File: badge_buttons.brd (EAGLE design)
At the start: 83 x 66 mm, 6 parts

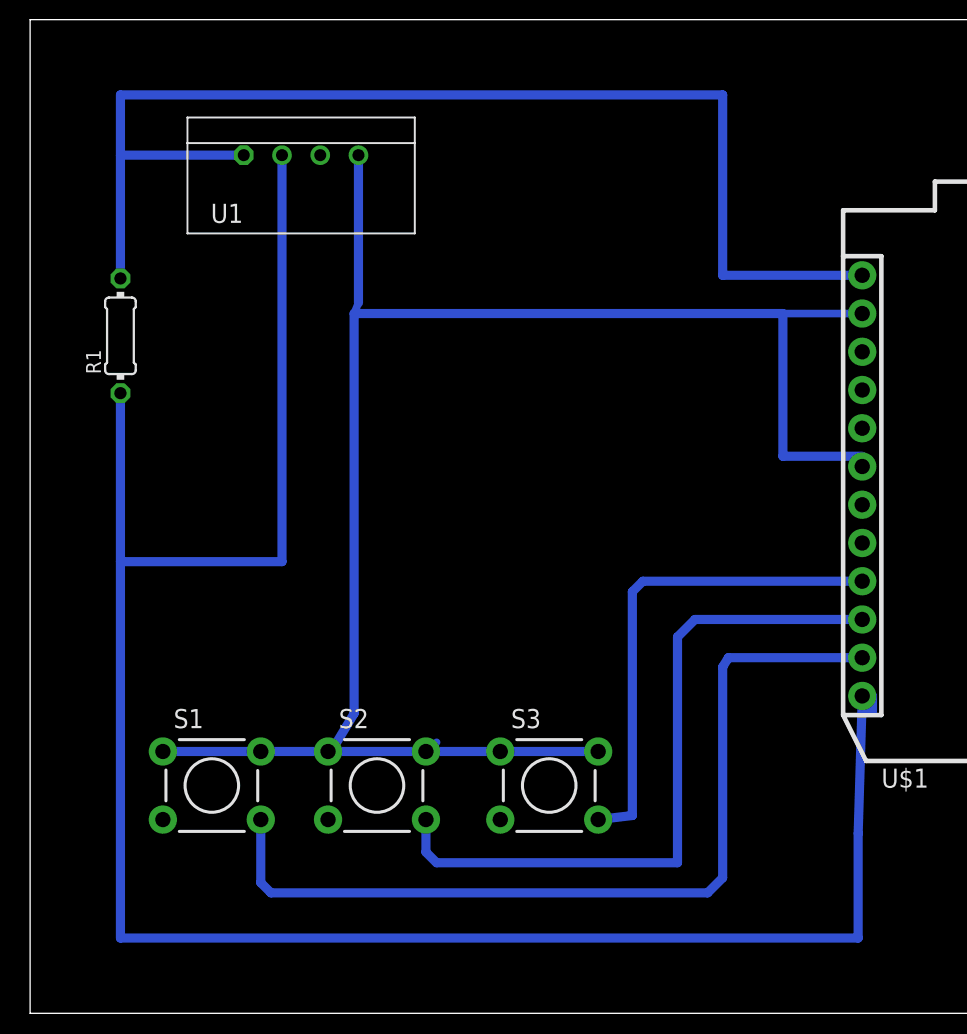
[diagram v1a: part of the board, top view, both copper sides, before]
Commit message: clean up lines, add sensor loop
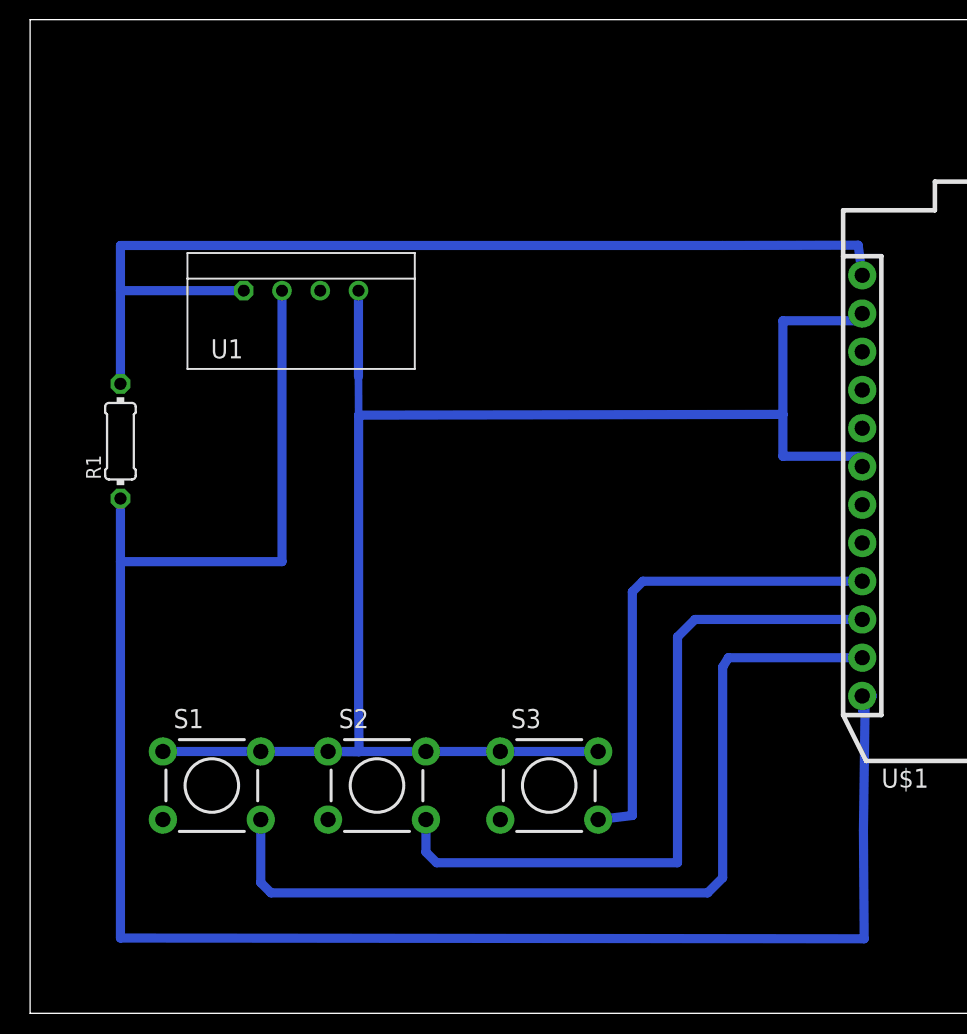
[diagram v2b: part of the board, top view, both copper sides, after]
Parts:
- moved U1 9.00 mm to (28.0, 58.0)
- moved R1 7.00 mm to (16.0, 48.0)
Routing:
- net N$6: track 142.2 -> 127.1 mm
- net N$5: track 81.6 -> 68.4 mm
- net N$4: track 119.1 -> 110.4 mm
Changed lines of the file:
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@@
 <setting verticaltext="up"/>
 </settings>
-<grid distance="1" unitdist="mm" unit="mm" style="lines" multiple="10" display="yes" altdistance="5" altunitdist="mil" altunit="mm"/>
+<grid distance="0.05" unitdist="mm" unit="mm" style="lines" multiple="10" display="yes" altdistance="0.1" altunitdist="mm" altunit="mm"/>
 <layers>
 <layer number="1" name="Top" color="4" fill="1" visible="yes" active="yes"/>
@@
 <element name="S3" library="SparkFun-Retired" package="TACTILE-PTH" value="" x="44.48" y="25.13"/>
 <element name="U$1" library="Particle-Devices" package="PHOTON" value="PHOTON_WITH_HEADERS" x="64" y="26"/>
-<element name="U1" library="RHT03_DHT-22_AM2302" package="RHT03_DHT-22" value="" x="28" y="67">
-<attribute name="PROD_ID" value="SEN-10167" x="28" y="67" size="1.778" layer="27" display="off"/>
+<element name="U1" library="RHT03_DHT-22_AM2302" package="RHT03_DHT-22" value="" x="28" y="58">
+<attribute name="PROD_ID" value="SEN-10167" x="28" y="58" size="1.778" layer="27" display="off"/>
 </element>
-<element name="R1" library="resistor" library_urn="urn:adsk.eagle:library:348" package="0204/7" package3d_urn="urn:adsk.eagle:package:25945/1" value="" x="16" y="55" rot="R90"/>
+<element name="R1" library="resistor" library_urn="urn:adsk.eagle:library:348" package="0204/7" package3d_urn="urn:adsk.eagle:package:25945/1" value="" x="16" y="48" rot="R90"/>
 </elements>
 <signals>
@@
 <wire x1="29.7888" y1="27.3906" x2="30" y2="27.3906" width="0.508" layer="16"/>
 <wire x1="30" y1="27.3906" x2="36.2912" y2="27.3906" width="0.6096" layer="16"/>
-<wire x1="37" y1="28" x2="36.3906" y2="27.3906" width="0.508" layer="16"/>
-<wire x1="36.3906" y1="27.3906" x2="36.2912" y2="27.3906" width="0.508" layer="16"/>
-<wire x1="36.2912" y1="27.3906" x2="41.2288" y2="27.3906" width="0.6096" layer="16"/>
+<wire x1="36.4" y1="27.3" x2="36.3906" y2="27.3906" width="0.508" layer="16"/>
+<wire x1="36.2912" y1="27.3906" x2="36.3906" y2="27.3906" width="0.6096" layer="16"/>
+<wire x1="36.3906" y1="27.3906" x2="41.2288" y2="27.3906" width="0.6096" layer="16"/>
 <wire x1="41.2288" y1="27.3906" x2="47.7312" y2="27.3906" width="0.6096" layer="16"/>
-<wire x1="31.81" y1="67" x2="31.81" y2="57.19" width="0.6096" layer="16"/>
-<wire x1="31.81" y1="57.19" x2="31.52" y2="56.48" width="0.508" layer="16"/>
-<wire x1="31.52" y1="56.48" x2="31.52" y2="29.9106" width="0.6096" layer="16"/>
-<wire x1="31.52" y1="29.9106" x2="30" y2="27.3906" width="0.6096" layer="16"/>
+<wire x1="31.81" y1="58" x2="31.81" y2="52.29" width="0.6096" layer="16"/>
+<wire x1="31.81" y1="52.29" x2="31.82" y2="49.73" width="0.508" layer="16"/>
+<wire x1="31.82" y1="49.73" x2="31.82" y2="30.0606" width="0.6096" layer="16"/>
+<wire x1="31.82" y1="30.0606" x2="31.85305" y2="27.371971875" width="0.6096" layer="16"/>
 <contactref element="U$1" pad="6"/>
-<wire x1="65.27" y1="56.48" x2="60" y2="56.48" width="0.508" layer="16"/>
-<wire x1="60" y1="56.48" x2="31.52" y2="56.48" width="0.6096" layer="16"/>
+<wire x1="31.85305" y1="27.371971875" x2="30" y2="27.3906" width="0.6096" layer="16"/>
+<wire x1="60" y1="49.78" x2="31.82" y2="49.73" width="0.6096" layer="16"/>
 <wire x1="65.27" y1="46.32" x2="65.27" y2="47" width="0.508" layer="16"/>
 <wire x1="65.27" y1="47" x2="60" y2="47" width="0.6096" layer="16"/>
-<wire x1="60" y1="47" x2="60" y2="56.48" width="0.6096" layer="16"/>
+<wire x1="60" y1="47" x2="60" y2="49.78" width="0.6096" layer="16"/>
+<wire x1="65.27" y1="56.48" x2="65.27" y2="56" width="0.6096" layer="16"/>
+<wire x1="65.27" y1="56" x2="60" y2="56" width="0.6096" layer="16"/>
+<wire x1="60" y1="56" x2="60" y2="49.78" width="0.6096" layer="16"/>
 </signal>
 <signal name="N$5">
@@
 <contactref element="U$1" pad="1"/>
 <contactref element="R1" pad="2"/>
-<wire x1="24.19" y1="67" x2="16" y2="67" width="0.6096" layer="16"/>
-<wire x1="16" y1="67" x2="16" y2="71" width="0.6096" layer="16"/>
-<wire x1="16" y1="71" x2="56" y2="71" width="0.6096" layer="16"/>
-<wire x1="56" y1="71" x2="56" y2="59.02" width="0.6096" layer="16"/>
-<wire x1="56" y1="59.02" x2="65.27" y2="59.02" width="0.6096" layer="16"/>
-<wire x1="16" y1="67" x2="16" y2="58.81" width="0.6096" layer="16"/>
+<wire x1="24.19" y1="58" x2="16" y2="58" width="0.6096" layer="16"/>
+<wire x1="16" y1="58" x2="16" y2="61" width="0.6096" layer="16"/>
+<wire x1="16" y1="61" x2="56" y2="61" width="0.6096" layer="16"/>
+<wire x1="56" y1="61" x2="65" y2="61.02" width="0.6096" layer="16"/>
+<wire x1="65" y1="61.02" x2="65.27" y2="59.02" width="0.6096" layer="16"/>
+<wire x1="16" y1="58" x2="16" y2="51.81" width="0.6096" layer="16"/>
 </signal>
 <signal name="N$6">
@@
 <contactref element="U$1" pad="12"/>
 <contactref element="R1" pad="1"/>
-<wire x1="26.73" y1="67" x2="26.73" y2="40" width="0.6096" layer="16"/>
+<wire x1="26.73" y1="58" x2="26.73" y2="40" width="0.6096" layer="16"/>
 <wire x1="26.73" y1="40" x2="16" y2="40" width="0.6096" layer="16"/>
 <wire x1="16" y1="40" x2="16" y2="15" width="0.6096" layer="16"/>
-<wire x1="16" y1="15" x2="65" y2="15" width="0.6096" layer="16"/>
+<wire x1="16" y1="15" x2="65.4" y2="14.95" width="0.6096" layer="16"/>
 <wire x1="66" y1="31.08" x2="65.27" y2="31.08" width="0.508" layer="16"/>
-<wire x1="65" y1="15" x2="65" y2="21.952" width="0.6096" layer="16"/>
-<wire x1="65" y1="21.952" x2="65.27" y2="30.952" width="0.6096" layer="16"/>
-<wire x1="65.27" y1="30.952" x2="65.27" y2="30.064" width="0.508" layer="16"/>
-<wire x1="65.27" y1="30.064" x2="66" y2="30.064" width="0.508" layer="16"/>
-<wire x1="66" y1="30.064" x2="66" y2="31.08" width="0.508" layer="16"/>
-<wire x1="16" y1="51.19" x2="16" y2="40" width="0.6096" layer="16"/>
+<wire x1="65.4" y1="14.95" x2="65.35" y2="22.152" width="0.6096" layer="16"/>
+<wire x1="65.35" y1="22.152" x2="65.47" y2="31.152" width="0.6096" layer="16"/>
+<wire x1="65.47" y1="31.152" x2="65.27" y2="30.064" width="0.508" layer="16"/>
+<wire x1="65.27" y1="30.064" x2="65.15" y2="30.964" width="0.508" layer="16"/>
+<wire x1="65.15" y1="30.964" x2="66" y2="31.08" width="0.508" layer="16"/>
+<wire x1="16" y1="44.19" x2="16" y2="40" width="0.6096" layer="16"/>
 </signal>
 </signals>

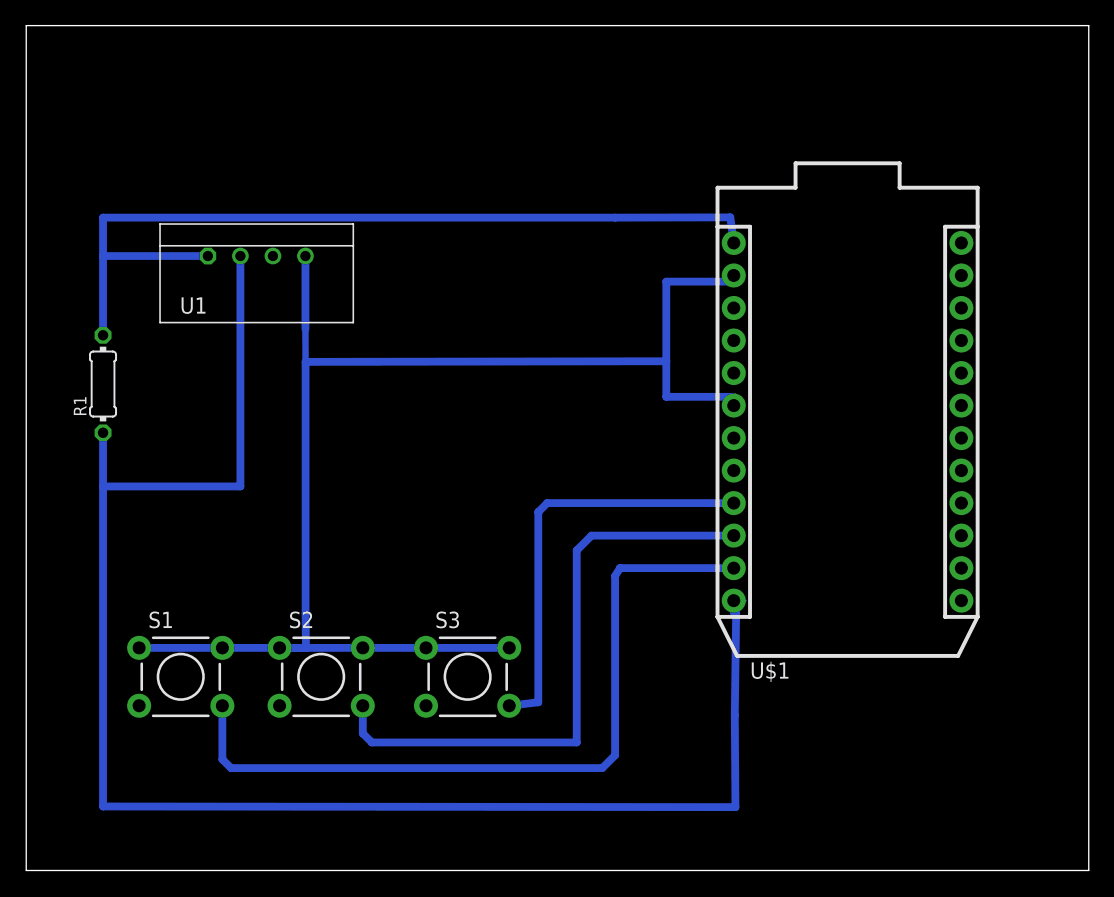
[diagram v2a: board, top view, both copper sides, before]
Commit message: fatten traces
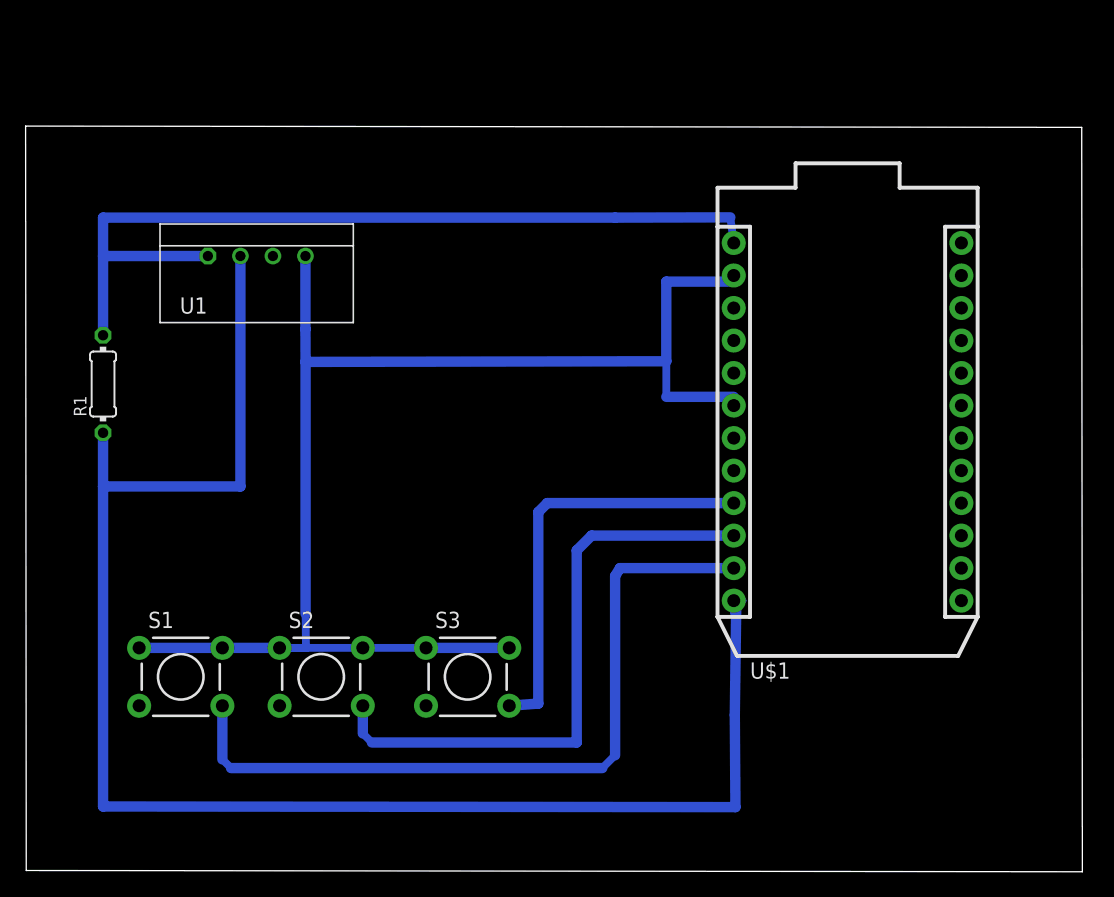
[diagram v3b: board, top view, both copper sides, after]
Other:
- board size 83 x 66 mm -> 82.5 x 58.3 mm
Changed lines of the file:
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@@
 <board>
 <plain>
-<wire x1="10" y1="10" x2="93" y2="10" width="0" layer="20"/>
-<wire x1="93" y1="10" x2="93" y2="76" width="0" layer="20"/>
-<wire x1="93" y1="76" x2="10" y2="76" width="0" layer="20"/>
-<wire x1="10" y1="76" x2="10" y2="10" width="0" layer="20"/>
+<wire x1="10" y1="10" x2="92.5" y2="9.9" width="0" layer="20"/>
+<wire x1="92.5" y1="9.9" x2="92.45" y2="68.05" width="0" layer="20"/>
+<wire x1="92.45" y1="68.05" x2="9.95" y2="68.15" width="0" layer="20"/>
+<wire x1="9.95" y1="68.15" x2="10" y2="10" width="0" layer="20"/>
 </plain>
 <attributes>
@@
 <wire x1="65.27" y1="38.7" x2="65" y2="38.97" width="0.3048" layer="16"/>
 <wire x1="65" y1="38.97" x2="65" y2="39" width="0.3048" layer="16"/>
-<wire x1="47.7312" y1="22.8694" x2="50" y2="23.1382" width="0.6096" layer="16"/>
-<wire x1="50" y1="23.1382" x2="50" y2="38" width="0.6096" layer="16"/>
-<wire x1="50" y1="38" x2="50.7" y2="38.7" width="0.6096" layer="16"/>
-<wire x1="50.7" y1="38.7" x2="65.27" y2="38.7" width="0.6096" layer="16"/>
+<wire x1="47.7312" y1="22.8694" x2="50" y2="23.0382" width="0.8128" layer="16"/>
+<wire x1="50" y1="23.0382" x2="50" y2="38" width="0.8128" layer="16"/>
+<wire x1="50" y1="38" x2="50.7" y2="38.7" width="0.8128" layer="16"/>
+<wire x1="50.7" y1="38.7" x2="65.27" y2="38.7" width="0.8128" layer="16"/>
 </signal>
 <signal name="N$2">
 <contactref element="S2" pad="4"/>
 <contactref element="U$1" pad="10"/>
-<wire x1="36.2912" y1="22.8694" x2="36.2912" y2="20.7088" width="0.6096" layer="16"/>
+<wire x1="36.2912" y1="22.8694" x2="36.2912" y2="20.7088" width="0.8128" layer="16"/>
 <wire x1="36.2912" y1="20.7088" x2="37" y2="20" width="0.6096" layer="16"/>
-<wire x1="37" y1="20" x2="53" y2="20" width="0.6096" layer="16"/>
-<wire x1="53" y1="20" x2="53" y2="35" width="0.6096" layer="16"/>
-<wire x1="54.16" y1="36.16" x2="65.27" y2="36.16" width="0.6096" layer="16"/>
-<wire x1="53" y1="35" x2="54.16" y2="36.16" width="0.6096" layer="16"/>
+<wire x1="37" y1="20" x2="53" y2="20" width="0.8128" layer="16"/>
+<wire x1="53" y1="20" x2="53" y2="35" width="0.8128" layer="16"/>
+<wire x1="54.16" y1="36.16" x2="65.27" y2="36.16" width="0.8128" layer="16"/>
+<wire x1="53" y1="35" x2="54.16" y2="36.16" width="0.8128" layer="16"/>
 </signal>
 <signal name="N$3">
 <contactref element="S1" pad="4"/>
 <contactref element="U$1" pad="11"/>
-<wire x1="25.3212" y1="22.8694" x2="25.3212" y2="18.6788" width="0.6096" layer="16"/>
+<wire x1="25.3212" y1="22.8694" x2="25.3212" y2="18.6788" width="0.8128" layer="16"/>
 <wire x1="25.3212" y1="18.6788" x2="26" y2="18" width="0.6096" layer="16"/>
-<wire x1="26" y1="18" x2="55" y2="18" width="0.6096" layer="16"/>
+<wire x1="26" y1="18" x2="55" y2="18" width="0.8128" layer="16"/>
 <wire x1="55" y1="18" x2="56" y2="19" width="0.6096" layer="16"/>
-<wire x1="56" y1="19" x2="56" y2="33" width="0.6096" layer="16"/>
-<wire x1="56" y1="33" x2="56.38" y2="33.62" width="0.6096" layer="16"/>
-<wire x1="56.38" y1="33.62" x2="65.27" y2="33.62" width="0.6096" layer="16"/>
+<wire x1="56" y1="19" x2="56" y2="33" width="0.8128" layer="16"/>
+<wire x1="56" y1="33" x2="56.38" y2="33.62" width="0.8128" layer="16"/>
+<wire x1="56.38" y1="33.62" x2="65.27" y2="33.62" width="0.8128" layer="16"/>
 </signal>
 <signal name="N$4">
@@
 <contactref element="S2" pad="2"/>
 <contactref element="S3" pad="2"/>
-<wire x1="18.8188" y1="27.3906" x2="25.3212" y2="27.3906" width="0.6096" layer="16"/>
-<wire x1="25.3212" y1="27.3906" x2="29.7888" y2="27.3906" width="0.6096" layer="16"/>
+<wire x1="18.8188" y1="27.3906" x2="25.3212" y2="27.3906" width="0.8128" layer="16"/>
+<wire x1="25.3212" y1="27.3906" x2="29.7888" y2="27.3906" width="0.8128" layer="16"/>
 <wire x1="29.7888" y1="27.3906" x2="30" y2="27.3906" width="0.508" layer="16"/>
 <wire x1="30" y1="27.3906" x2="36.2912" y2="27.3906" width="0.6096" layer="16"/>
@@
 <wire x1="36.2912" y1="27.3906" x2="36.3906" y2="27.3906" width="0.6096" layer="16"/>
 <wire x1="36.3906" y1="27.3906" x2="41.2288" y2="27.3906" width="0.6096" layer="16"/>
-<wire x1="41.2288" y1="27.3906" x2="47.7312" y2="27.3906" width="0.6096" layer="16"/>
-<wire x1="31.81" y1="58" x2="31.81" y2="52.29" width="0.6096" layer="16"/>
-<wire x1="31.81" y1="52.29" x2="31.82" y2="49.73" width="0.508" layer="16"/>
-<wire x1="31.82" y1="49.73" x2="31.82" y2="30.0606" width="0.6096" layer="16"/>
+<wire x1="41.2288" y1="27.3906" x2="47.7312" y2="27.3906" width="0.8128" layer="16"/>
+<wire x1="31.81" y1="58" x2="31.81" y2="52.29" width="0.8128" layer="16"/>
+<wire x1="31.81" y1="52.29" x2="31.82" y2="49.73" width="0.8128" layer="16"/>
+<wire x1="31.82" y1="49.73" x2="31.82" y2="30.0606" width="0.8128" layer="16"/>
 <wire x1="31.82" y1="30.0606" x2="31.85305" y2="27.371971875" width="0.6096" layer="16"/>
 <contactref element="U$1" pad="6"/>
 <wire x1="31.85305" y1="27.371971875" x2="30" y2="27.3906" width="0.6096" layer="16"/>
-<wire x1="60" y1="49.78" x2="31.82" y2="49.73" width="0.6096" layer="16"/>
+<wire x1="60" y1="49.78" x2="31.82" y2="49.73" width="0.8128" layer="16"/>
 <wire x1="65.27" y1="46.32" x2="65.27" y2="47" width="0.508" layer="16"/>
-<wire x1="65.27" y1="47" x2="60" y2="47" width="0.6096" layer="16"/>
+<wire x1="65.27" y1="47" x2="60" y2="47" width="0.8128" layer="16"/>
 <wire x1="60" y1="47" x2="60" y2="49.78" width="0.6096" layer="16"/>
 <wire x1="65.27" y1="56.48" x2="65.27" y2="56" width="0.6096" layer="16"/>
-<wire x1="65.27" y1="56" x2="60" y2="56" width="0.6096" layer="16"/>
-<wire x1="60" y1="56" x2="60" y2="49.78" width="0.6096" layer="16"/>
+<wire x1="65.27" y1="56" x2="60" y2="56" width="0.8128" layer="16"/>
+<wire x1="60" y1="56" x2="60" y2="49.78" width="0.8128" layer="16"/>
 </signal>
 <signal name="N$5">
@@
 <contactref element="U$1" pad="1"/>
 <contactref element="R1" pad="2"/>
-<wire x1="24.19" y1="58" x2="16" y2="58" width="0.6096" layer="16"/>
-<wire x1="16" y1="58" x2="16" y2="61" width="0.6096" layer="16"/>
-<wire x1="16" y1="61" x2="56" y2="61" width="0.6096" layer="16"/>
-<wire x1="56" y1="61" x2="65" y2="61.02" width="0.6096" layer="16"/>
+<wire x1="24.19" y1="58" x2="16" y2="58" width="0.8128" layer="16"/>
+<wire x1="16" y1="58" x2="16" y2="61" width="0.8128" layer="16"/>
+<wire x1="16" y1="61" x2="56" y2="61" width="0.8128" layer="16"/>
+<wire x1="56" y1="61" x2="65" y2="61.02" width="0.8128" layer="16"/>
 <wire x1="65" y1="61.02" x2="65.27" y2="59.02" width="0.6096" layer="16"/>
-<wire x1="16" y1="58" x2="16" y2="51.81" width="0.6096" layer="16"/>
+<wire x1="16" y1="58" x2="16" y2="51.81" width="0.8128" layer="16"/>
 </signal>
 <signal name="N$6">
@@
 <contactref element="U$1" pad="12"/>
 <contactref element="R1" pad="1"/>
-<wire x1="26.73" y1="58" x2="26.73" y2="40" width="0.6096" layer="16"/>
-<wire x1="26.73" y1="40" x2="16" y2="40" width="0.6096" layer="16"/>
-<wire x1="16" y1="40" x2="16" y2="15" width="0.6096" layer="16"/>
-<wire x1="16" y1="15" x2="65.4" y2="14.95" width="0.6096" layer="16"/>
+<wire x1="26.73" y1="58" x2="26.73" y2="40" width="0.8128" layer="16"/>
+<wire x1="26.73" y1="40" x2="16" y2="40" width="0.8128" layer="16"/>
+<wire x1="16" y1="40" x2="16" y2="15" width="0.8128" layer="16"/>
+<wire x1="16" y1="15" x2="65.4" y2="14.95" width="0.8128" layer="16"/>
 <wire x1="66" y1="31.08" x2="65.27" y2="31.08" width="0.508" layer="16"/>
-<wire x1="65.4" y1="14.95" x2="65.35" y2="22.152" width="0.6096" layer="16"/>
-<wire x1="65.35" y1="22.152" x2="65.47" y2="31.152" width="0.6096" layer="16"/>
+<wire x1="65.4" y1="14.95" x2="65.35" y2="22.152" width="0.8128" layer="16"/>
+<wire x1="65.35" y1="22.152" x2="65.47" y2="31.152" width="0.8128" layer="16"/>
 <wire x1="65.47" y1="31.152" x2="65.27" y2="30.064" width="0.508" layer="16"/>
 <wire x1="65.27" y1="30.064" x2="65.15" y2="30.964" width="0.508" layer="16"/>
 <wire x1="65.15" y1="30.964" x2="66" y2="31.08" width="0.508" layer="16"/>
-<wire x1="16" y1="44.19" x2="16" y2="40" width="0.6096" layer="16"/>
+<wire x1="16" y1="44.19" x2="16" y2="40" width="0.8128" layer="16"/>
 </signal>
 </signals>
